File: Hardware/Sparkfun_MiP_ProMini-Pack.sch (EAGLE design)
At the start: 45 parts, among them Q1 8MHz, U1 ATMEGA328, U2 MIC5205, U3 TS3USB221A

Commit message: renamed files
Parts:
- added FID1, FID2: FIDUCIAL1X2, SparkFun-Aesthetics:FIDUCIAL1X2
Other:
- note added: "v10"
- note removed: "v01"
- moved on the sheet: R2
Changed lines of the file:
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@@
 <part name="GND32" library="SparkFun" deviceset="GND" device=""/>
 <part name="P+8" library="SparkFun" deviceset="3.3V" device="" value="VCC"/>
+<part name="FID1" library="SparkFun-Aesthetics" deviceset="FIDUCIAL" device="1X2"/>
+<part name="FID2" library="SparkFun-Aesthetics" deviceset="FIDUCIAL" device="1X2"/>
 </parts>
 <sheets>
@@
 <text x="241.3" y="141.478" size="1.778" layer="97" rot="R90">Optional Pullups for I2C lines</text>
 <text x="167.64" y="10.16" size="2.54" layer="94">Casey Kuhns</text>
-<text x="238.76" y="7.62" size="2.54" layer="94">v01</text>
+<text x="238.76" y="7.62" size="2.54" layer="94">v10</text>
 </plain>
 <instances>
-<instance part="R2" gate="G$1" x="139.7" y="165.1" rot="R90"/>
+<instance part="R2" gate="G$1" x="142.24" y="165.1" rot="R90"/>
 <instance part="GND3" gate="1" x="139.7" y="139.7"/>
 <instance part="C3" gate="G$1" x="152.4" y="106.68" smashed="yes" rot="R180">
@@
 </instance>
 <instance part="GND8" gate="1" x="215.9" y="71.12"/>
-<instance part="P+11" gate="G$1" x="139.7" y="172.72"/>
+<instance part="P+11" gate="G$1" x="142.24" y="172.72"/>
 <instance part="P+15" gate="G$1" x="152.4" y="111.76" smashed="yes">
 <attribute name="VALUE" x="148.844" y="115.316" size="1.778" layer="96"/>
@@
 <attribute name="VALUE" x="170.18" y="93.98" size="1.778" layer="96"/>
 </instance>
-<instance part="P+1" gate="G$1" x="162.56" y="160.02"/>
+<instance part="P+1" gate="G$1" x="162.56" y="172.72"/>
 <instance part="GND5" gate="1" x="162.56" y="96.52"/>
 <instance part="JP1" gate="G$1" x="17.78" y="165.1"/>
@@
 <instance part="GND32" gate="1" x="63.5" y="86.36"/>
 <instance part="P+8" gate="G$1" x="114.3" y="104.14"/>
+<instance part="FID1" gate="G$1" x="246.38" y="25.4"/>
+<instance part="FID2" gate="G$1" x="241.3" y="25.4"/>
 </instances>
 <busses>
@@
 </segment>
 <segment>
-<wire x1="165.1" y1="157.48" x2="139.7" y2="157.48" width="0.1524" layer="91"/>
-<wire x1="139.7" y1="160.02" x2="139.7" y2="157.48" width="0.1524" layer="91"/>
-<wire x1="139.7" y1="154.94" x2="139.7" y2="157.48" width="0.1524" layer="91"/>
-<wire x1="139.7" y1="157.48" x2="134.62" y2="157.48" width="0.1524" layer="91"/>
-<junction x="139.7" y="157.48"/>
+<wire x1="165.1" y1="157.48" x2="142.24" y2="157.48" width="0.1524" layer="91"/>
+<wire x1="142.24" y1="160.02" x2="142.24" y2="157.48" width="0.1524" layer="91"/>
+<wire x1="142.24" y1="157.48" x2="139.7" y2="157.48" width="0.1524" layer="91"/>
+<junction x="142.24" y="157.48"/>
 <label x="149.86" y="157.48" size="1.778" layer="95"/>
 <pinref part="U1" gate="G$1" pin="PC6(/RESET)"/>
@@
 <pinref part="C2" gate="G$1" pin="1"/>
 <pinref part="S1" gate="G$1" pin="2"/>
+<wire x1="139.7" y1="157.48" x2="134.62" y2="157.48" width="0.1524" layer="91"/>
+<wire x1="139.7" y1="154.94" x2="139.7" y2="157.48" width="0.1524" layer="91"/>
+<junction x="139.7" y="157.48"/>
 </segment>
 </net>
@@
 <net name="VCC" class="0">
 <segment>
-<wire x1="139.7" y1="172.72" x2="139.7" y2="170.18" width="0.1524" layer="91"/>
+<wire x1="142.24" y1="172.72" x2="142.24" y2="170.18" width="0.1524" layer="91"/>
 <pinref part="R2" gate="G$1" pin="2"/>
 <pinref part="P+11" gate="G$1" pin="3.3V"/>
@@
 <segment>
 <wire x1="165.1" y1="152.4" x2="162.56" y2="152.4" width="0.1524" layer="91"/>
-<wire x1="162.56" y1="152.4" x2="162.56" y2="160.02" width="0.1524" layer="91"/>
+<wire x1="162.56" y1="152.4" x2="162.56" y2="172.72" width="0.1524" layer="91"/>
 <wire x1="165.1" y1="149.86" x2="162.56" y2="149.86" width="0.1524" layer="91"/>
 <wire x1="162.56" y1="149.86" x2="162.56" y2="152.4" width="0.1524" layer="91"/>

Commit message: addressing issues in github
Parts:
- R1, R3: value (none) -> DNP
- SJ5: value JUMPER-PAD-2-NC_BY_TRACE -> D2 Jumper
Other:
- note added: "Arduino Pro-Mini"
- note added: "Expansion Headers"
- note added: "MiP UART"
- note added: "Note: Cut jumper to move SEL to another pin"
- note added: "Programming Port"
- note added: "UART Selection MiP <-> Programming Port"
- note added: "VIN - Battery Voltage (4.8V - 6V) VCC - 3.3V"
- moved on the sheet: C10, C13, C19, JP2, JP3, JP4, JP5, JP6, JP7, JP8, JP9, R3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

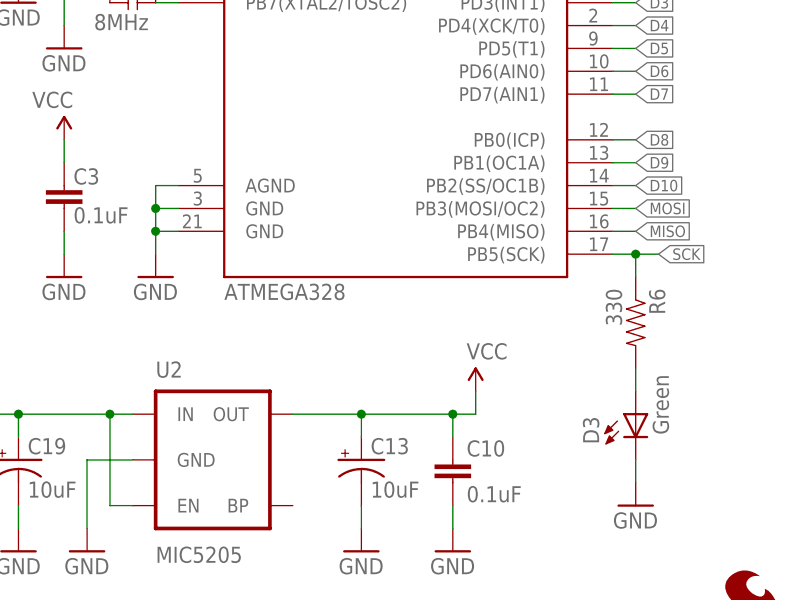
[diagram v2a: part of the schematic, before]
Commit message: added ProdID's  to parts
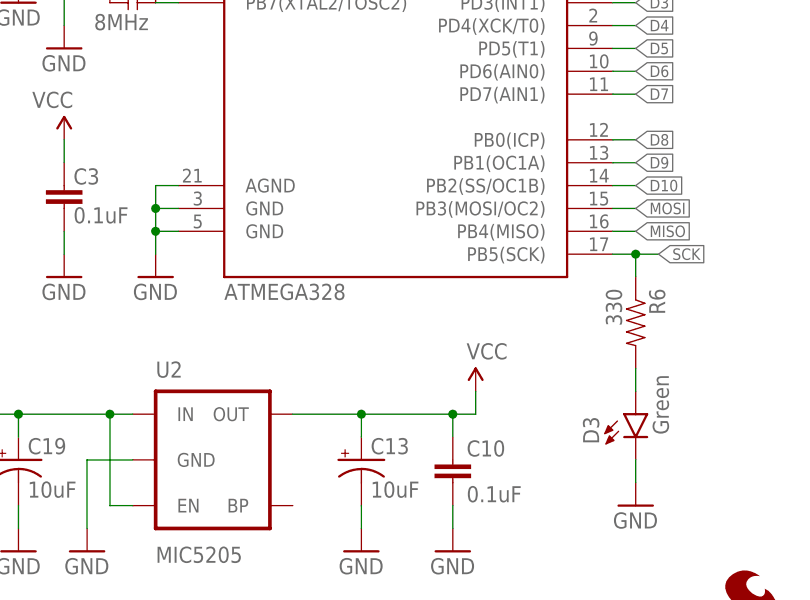
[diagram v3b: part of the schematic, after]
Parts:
- C1, C10, C2, C3, C4: device SparkFun:CAP0603-CAP -> SparkFun-Capacitors:0.1UF-25V(+80/-20%)(0603)
- D3: device Testing:LED -> SparkFun-LED:LED-GREEN0603
- R6: device SparkFun:RESISTOR0603-RES -> SparkFun-Resistors:330OHM1/10W1%(0603)
- S1: device Testing:SWITCH-MOMENTARY-2SMD-ALT01 -> SparkFun-Electromechanical:SWITCH-MOMENTARY-2SMD
- U1: device SparkFun:ATMEGA168 -> SparkFun-DigitalIC:ATMEGA328_SMT
- U2: device SparkFun:V_REG_LDOSMD -> SparkFun-PowerIC:MIC52053.3V
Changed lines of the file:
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@@
 <?xml version="1.0" encoding="utf-8"?>
 <!DOCTYPE eagle SYSTEM "eagle.dtd">
-<eagle version="6.6.0">
+<eagle version="6.5.0">
 <drawing>
 <settings>
@@
 <part name="R2" library="SparkFun" deviceset="RESISTOR" device="0603-RES" value="10K"/>
 <part name="GND3" library="SparkFun" deviceset="GND" device=""/>
-<part name="C3" library="SparkFun" deviceset="CAP" device="0603-CAP" value="0.1uF"/>
+<part name="C3" library="SparkFun-Capacitors" deviceset="0.1UF-25V(+80/-20%)(0603)" device="" value="0.1uF"/>
 <part name="GND2" library="SparkFun" deviceset="GND" device=""/>
-<part name="C1" library="SparkFun" deviceset="CAP" device="0603-CAP" value="0.1uF"/>
+<part name="C1" library="SparkFun-Capacitors" deviceset="0.1UF-25V(+80/-20%)(0603)" device="" value="0.1uF"/>
 <part name="GND7" library="SparkFun" deviceset="GND" device=""/>
-<part name="R6" library="SparkFun" deviceset="RESISTOR" device="0603-RES" value="330"/>
-<part name="D3" library="Testing" deviceset="LED" device="" value="Green"/>
+<part name="R6" library="SparkFun-Resistors" deviceset="330OHM1/10W1%(0603)" device="" value="330"/>
+<part name="D3" library="SparkFun-LED" deviceset="LED-GREEN" device="0603" value="Green"/>
 <part name="GND8" library="SparkFun" deviceset="GND" device=""/>
 <part name="P+11" library="SparkFun" deviceset="3.3V" device="" value="VCC"/>
@@
 <part name="GND4" library="SparkFun" deviceset="GND" device=""/>
 <part name="JP2" library="SparkFun" deviceset="M02" device="PTH"/>
-<part name="U1" library="SparkFun" deviceset="ATMEGA168" device="" value="ATMEGA328"/>
+<part name="U1" library="SparkFun-DigitalIC" deviceset="ATMEGA328_SMT" device="" value="ATMEGA328"/>
 <part name="P+1" library="SparkFun" deviceset="3.3V" device="" value="VCC"/>
 <part name="GND5" library="SparkFun" deviceset="GND" device=""/>
 <part name="JP1" library="SparkFun" deviceset="ARDUINO_SERIAL_PROGRAM" device="PTH" value="FTDI Basic"/>
-<part name="C2" library="SparkFun" deviceset="CAP" device="0603-CAP" value="0.1uF"/>
+<part name="C2" library="SparkFun-Capacitors" deviceset="0.1UF-25V(+80/-20%)(0603)" device="" value="0.1uF"/>
 <part name="R1" library="SparkFun" deviceset="RESISTOR" device="0603-RES" value="DNP"/>
 <part name="R3" library="SparkFun" deviceset="RESISTOR" device="0603-RES" value="DNP"/>
 <part name="P+2" library="SparkFun" deviceset="3.3V" device="" value="VCC"/>
 <part name="P+3" library="SparkFun" deviceset="3.3V" device="" value="VCC"/>
-<part name="S1" library="Testing" deviceset="SWITCH-MOMENTARY-2" device="SMD-ALT01" value="Reset"/>
+<part name="S1" library="SparkFun-Electromechanical" deviceset="SWITCH-MOMENTARY-2" device="SMD" value="Reset"/>
 <part name="JP3" library="SparkFun" deviceset="M02" device="PTH"/>
 <part name="Q1" library="SparkFun-FreqCtrl" deviceset="RESONATOR" device="8MHZ" value="8MHz"/>
@@
 <part name="R11" library="SparkFun-Resistors" deviceset="1KOHM1/10W1%(0603)" device="" value="1K"/>
 <part name="P+6" library="SparkFun" deviceset="3.3V" device="" value="VCC"/>
-<part name="C4" library="SparkFun" deviceset="CAP" device="0603-CAP" value="0.1uF"/>
+<part name="C4" library="SparkFun-Capacitors" deviceset="0.1UF-25V(+80/-20%)(0603)" device="" value="0.1uF"/>
 <part name="GND12" library="SparkFun" deviceset="GND" device=""/>
 <part name="P+7" library="SparkFun" deviceset="3.3V" device="" value="VCC"/>
@@
 <part name="SJ1" library="SparkFun-Passives" deviceset="JUMPER-PAD-3-2OF3_NC_BY_PASTE" device="" value=""/>
 <part name="SJ3" library="SparkFun-Passives" deviceset="JUMPER-PAD-3-2OF3_NC_BY_PASTE" device="" value=""/>
-<part name="C10" library="SparkFun" deviceset="CAP" device="0603-CAP" value="0.1uF"/>
+<part name="C10" library="SparkFun-Capacitors" deviceset="0.1UF-25V(+80/-20%)(0603)" device="" value="0.1uF"/>
 <part name="C13" library="SparkFun" deviceset="CAP_POL" device="1206" value="10uF"/>
 <part name="GND25" library="SparkFun" deviceset="GND" device=""/>
 <part name="GND26" library="SparkFun" deviceset="GND" device=""/>
-<part name="U2" library="SparkFun" deviceset="V_REG_LDO" device="SMD" value="MIC5205"/>
+<part name="U2" library="SparkFun-PowerIC" deviceset="MIC5205" device="3.3V" value="MIC5205"/>
 <part name="C19" library="SparkFun" deviceset="CAP_POL" device="1206" value="10uF"/>
 <part name="GND30" library="SparkFun" deviceset="GND" device=""/>
